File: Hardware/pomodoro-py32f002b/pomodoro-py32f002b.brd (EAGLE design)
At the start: 38 x 69 mm, 42 parts, among them Q1 IRLML2502TRPBF, Q2 IRLML2502TRPBF, Q3 IRLML2502TRPBF, Q4 DMG2305UX-7

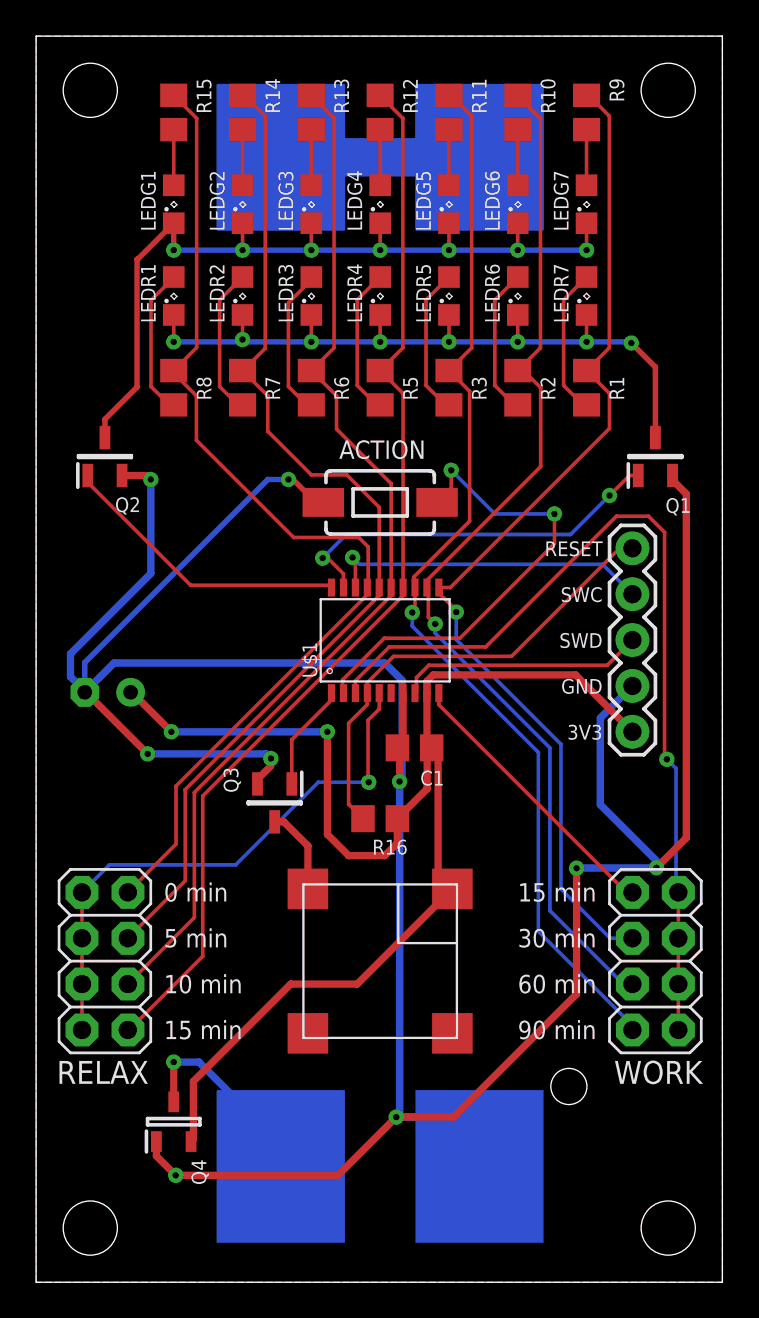
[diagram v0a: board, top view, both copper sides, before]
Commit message: Reduce current on sleep by disabling outputs, updated hardware, rounded corners, changed leds from 0805 to 0603
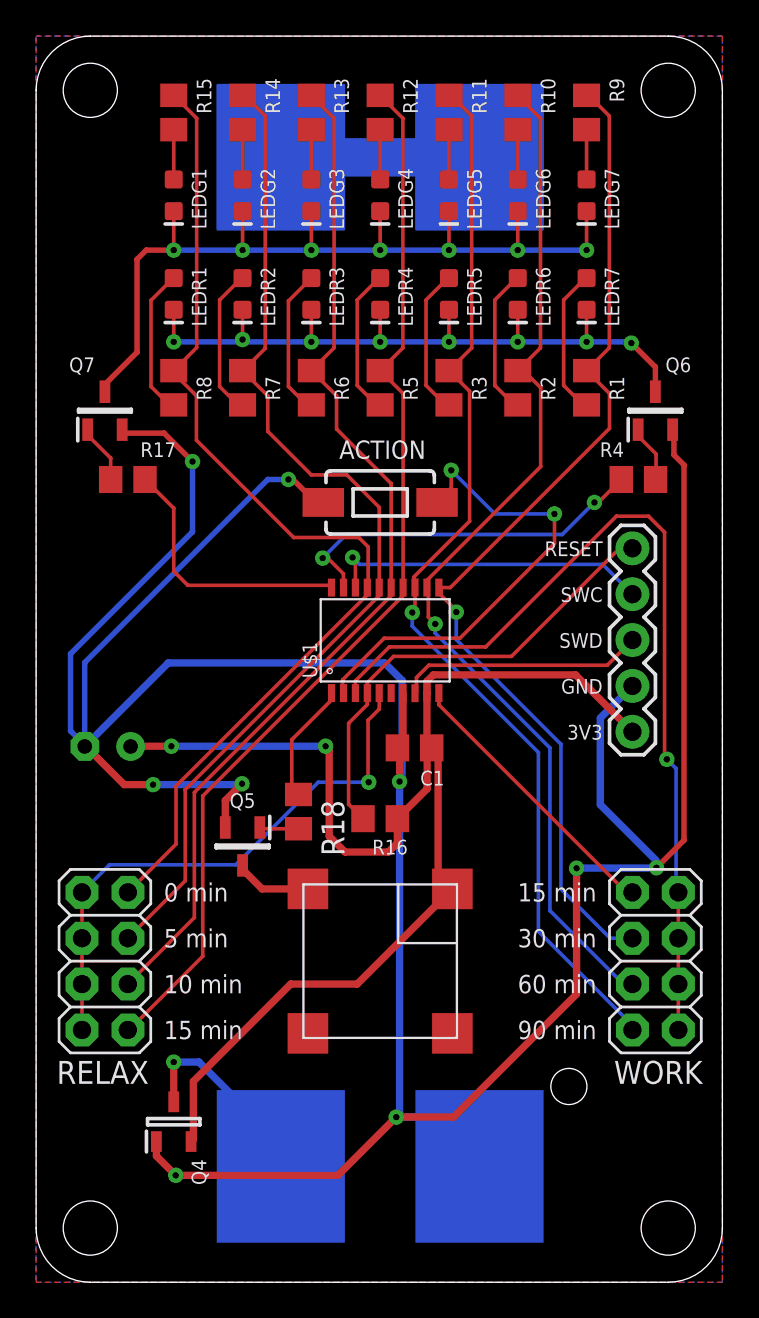
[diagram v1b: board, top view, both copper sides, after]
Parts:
- removed Q1, Q2, Q3: IRLML2502TRPBF, IRLML2502TRPBF:SOT95P237X112-3N
- added Q5, Q6, Q7: MMBT3904LT3G, MMBT3904LT3G:SOT96P237X111-3N
- added R17: 10K, rcl:R0805
- added R18, R4: 10k, rcl:R0805
- LEDG1, LEDG2, LEDG3, LEDG4, LEDG5, LEDG6, LEDG7, LEDR1, LEDR2, LEDR3, LEDR4, LEDR5, LEDR6, LEDR7: device led:SML0805 -> SparkFun-LED:LED-0603
- moved C2 3.00 mm to (3.96, 29.7)
- moved LEDG1 0.50 mm to (7.62, 60.2), turned to 270 degrees
- moved LEDG2 0.50 mm to (11.4, 60.2), turned to 270 degrees
- moved LEDG3 0.50 mm to (15.2, 60.2), turned to 270 degrees
- moved LEDG4 0.50 mm to (19.1, 60.2), turned to 270 degrees
- moved LEDG5 0.50 mm to (22.9, 60.2), turned to 270 degrees
- moved LEDG6 0.50 mm to (26.7, 60.2), turned to 270 degrees
- moved LEDG7 0.50 mm to (30.5, 60.2), turned to 270 degrees
- moved LEDR1 0.12 mm to (7.62, 54.7), turned to 270 degrees
- moved LEDR2 0.12 mm to (11.4, 54.7), turned to 270 degrees
- moved LEDR3 0.12 mm to (15.2, 54.7), turned to 270 degrees
- moved LEDR4 0.12 mm to (19.1, 54.7), turned to 270 degrees
- moved LEDR5 0.12 mm to (22.9, 54.7), turned to 270 degrees
- moved LEDR6 0.12 mm to (26.7, 54.7), turned to 270 degrees
- moved LEDR7 0.12 mm to (30.5, 54.7), turned to 270 degrees
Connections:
- new net N$16: Q6.1, R4.2
- new net N$19: Q5.1, R18.2
- new net N$6: Q7.1, R17.2
- net BIN: now also R4.1; no longer Q1.1
- net BIN1: now also R17.1; no longer Q2.1
- net GND: now also Q5.2, Q6.2, Q7.2; no longer Q1.2, Q2.2, Q3.2
- net N$10: now also Q7.3; no longer Q2.3
- net N$17: now also Q5.3; no longer Q3.3
- net N$26: now also R18.1; no longer Q3.1
- net N$40: now also Q6.3; no longer Q1.3
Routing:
- net GND: track 177.4 -> 190.9 mm
- net N$6: track 0.00 -> 3.29 mm
- net N$16: track 0.00 -> 3.18 mm
- net N$19: track 0.00 -> 2.17 mm
- net +3V3: track 75.3 -> 73.3 mm
- net N$10: track 46.8 -> 48.3 mm
- net BIN1: track 16.3 -> 14.9 mm
- net BIN: track 21.6 -> 20.6 mm
- net N$26: track 5.94 -> 6.68 mm
- net N$40: track 41.6 -> 41.1 mm
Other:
- outline, holes or cut-outs redrawn
- board text added: "Pomodoro Timer v1.0 RevB PY32"
- board text removed: "Pomodoro Timer v1.0 RevB"
